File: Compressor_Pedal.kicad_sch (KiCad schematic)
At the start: 14 parts, among them J1 AudioJack2, J2 AudioJack2, U3 LM358, U4 LM358

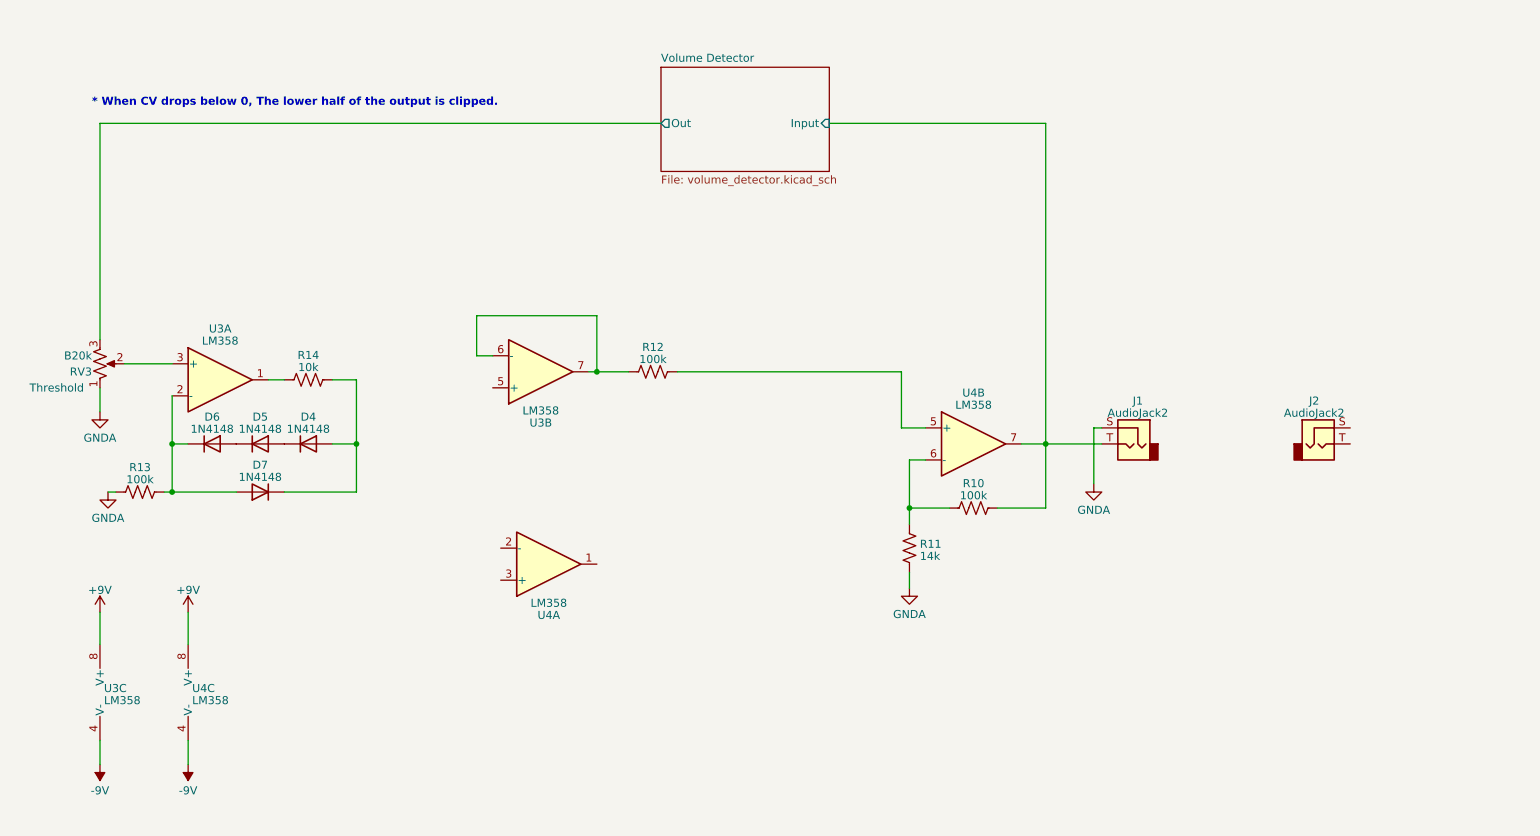
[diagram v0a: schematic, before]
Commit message: schematic finished, begin layout
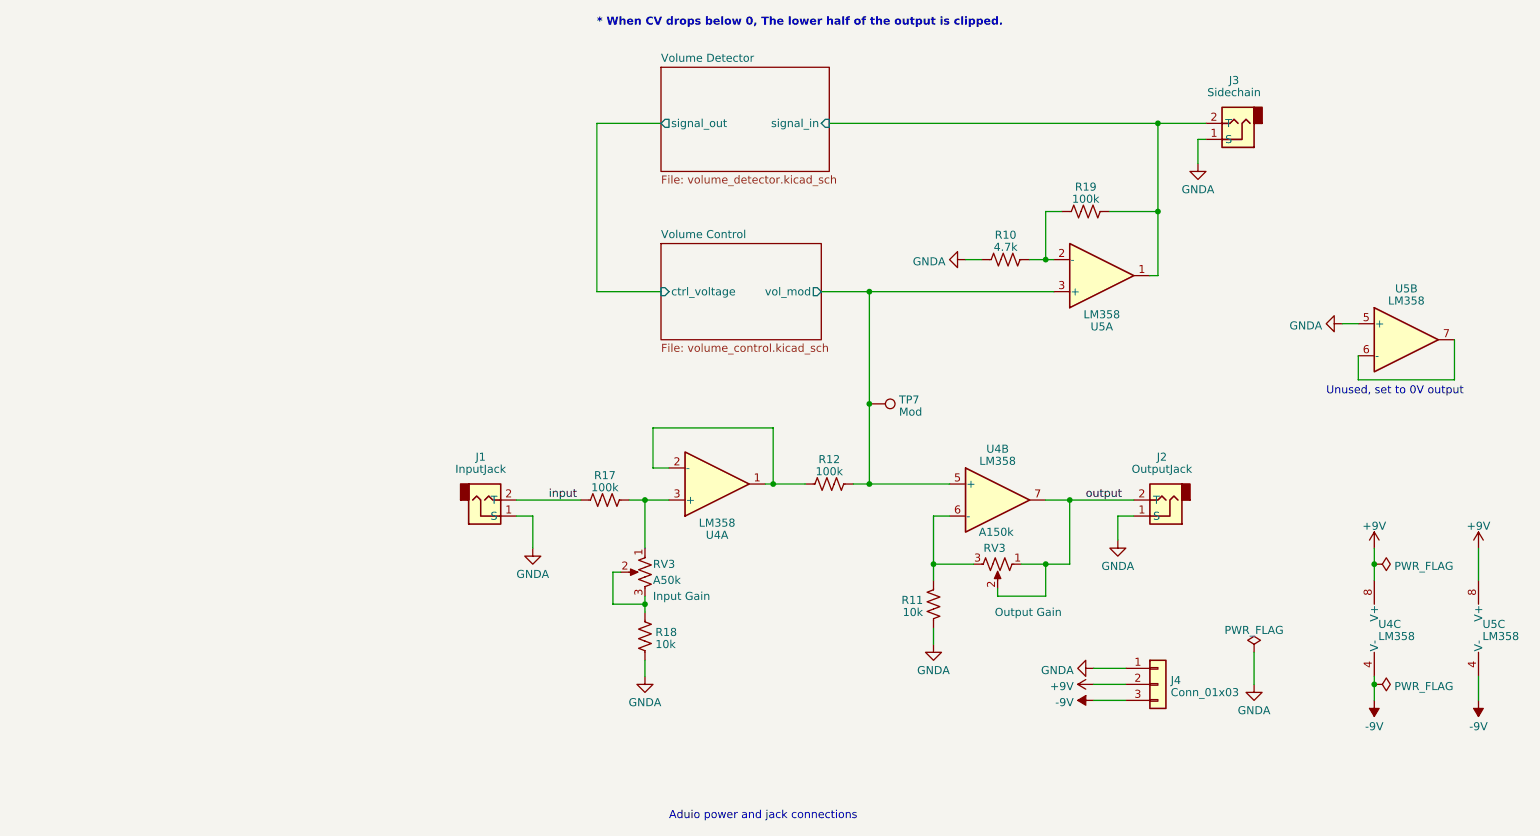
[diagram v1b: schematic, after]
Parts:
- removed D4, D5, D6, D7: 1N4148, Diode_THT:D_DO-35_SOD27_P7.62mm_Horizontal, symbol Diode:1N4148
- removed R13: 100k, symbol Device:R_US
- removed R14: 10k, symbol Device:R_US
- removed RV3: B20k, symbol Device:R_Potentiometer_US
- removed U3: LM358, symbol Amplifier_Operational:LM358
- added J3: Sidechain, TestPoint:TestPoint_2Pads_Pitch5.08mm_Drill1.3mm, symbol Connector_Audio:AudioJack2
- added J4: Conn_01x03, symbol Connector_Generic:Conn_01x03
- added R17, R19: 100k, Resistor_THT:R_Axial_DIN0207_L6.3mm_D2.5mm_P2.54mm_Vertical, symbol Device:R_US
- added R18: 10k, Resistor_THT:R_Axial_DIN0207_L6.3mm_D2.5mm_P2.54mm_Vertical, symbol Device:R_US
- added RV3: A150k, Potentiometer_THT:Potentiometer_Alps_RK163_Single_Horizontal, symbol Device:R_Potentiometer_US
- added RV3: A50k, Potentiometer_THT:Potentiometer_Alps_RK163_Single_Horizontal, symbol Device:R_Potentiometer_US
- added TP7: Mod, Connector_Pin:Pin_D1.3mm_L10.0mm_W3.5mm_Flat, symbol Connector:TestPoint
- added U5: LM358, Package_DIP:DIP-8_W7.62mm_Socket_LongPads, symbol Amplifier_Operational:LM358
- J1: renamed from J2; value AudioJack2 -> InputJack; footprint (none) -> TestPoint:TestPoint_2Pads_Pitch5.08mm_Drill1.3mm
- J2: renamed from J1; value AudioJack2 -> OutputJack; footprint (none) -> TestPoint:TestPoint_2Pads_Pitch5.08mm_Drill1.3mm
- R10: value 100k -> 4.7k; footprint (none) -> Resistor_THT:R_Axial_DIN0207_L6.3mm_D2.5mm_P2.54mm_Vertical
- R11: value 14k -> 10k; footprint (none) -> Resistor_THT:R_Axial_DIN0207_L6.3mm_D2.5mm_P2.54mm_Vertical
- R12: footprint (none) -> Resistor_THT:R_Axial_DIN0207_L6.3mm_D2.5mm_P2.54mm_Vertical
- U4: footprint (none) -> Package_DIP:DIP-8_W7.62mm_Socket_LongPads
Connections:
- net +9V: now also J4.2 (Pin_2), U5.8 (V+)
- net -9V: now also J4.3 (Pin_3), U5.4 (V-)
- net GNDA: now also J1.1 (S), J2.1 (S), R10.1, J3.1 (S), J4.1 (Pin_1), R18.1, U5.5 (+); no longer J2.S
- net at U4.1: now also R12.1, U4.2 (-)
- net at U4.3 (+): now also R17.2, RV3.1
- net Volume Control/vol_mod: now reaches R12.2, U4.5 (+)
- net Volume Control/vol_mod: now also TP7.1, U5.3 (+)
- net at R11.2, U4.6 (-): now also RV3.3; no longer R10.1
- removed net Volume Detector/Input: J2.T, R10.2, U4.7
- new net: R10.2, R19.1, U5.2 (-)
- new net: R18.2, RV3.2, RV3.3
- new net: U5.6 (-), U5.7
- new net Volume Detector/signal_in: J3.2 (T), R19.2, U5.1
- new net input: J1.2 (T), R17.1
- new net output: J2.2 (T), RV3.1, RV3.2, U4.7
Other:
- added sheet Volume Control (volume_control.kicad_sch)
- sheet Volume Detector ports: added signal_in, signal_out; removed Input, Out
- note added: "Aduio power and jack connections"
- note added: "Unused, set to 0V output"
- moved on the sheet: R11, R12, U4A, U4B, U4C

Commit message: sent for build
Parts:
- added JP1, JP2: Jumper_2_Bridged, TestPoint:TestPoint_2Pads_Pitch2.54mm_Drill0.8mm, symbol Jumper:Jumper_2_Bridged
- added TP10: MOD_IN, Connector_Pin:Pin_D0.9mm_L10.0mm_W2.4mm_FlatFork, symbol Connector:TestPoint
- added TP8: AIN, Connector_Pin:Pin_D0.9mm_L10.0mm_W2.4mm_FlatFork, symbol Connector:TestPoint
- added TP9: AOUT, Connector_Pin:Pin_D0.9mm_L10.0mm_W2.4mm_FlatFork, symbol Connector:TestPoint
- J4: footprint (none) -> Connector_PinHeader_2.54mm:PinHeader_1x03_P2.54mm_Vertical
- TP7: value Mod -> MOD_OUT; footprint Connector_Pin:Pin_D1.3mm_L10.0mm_W3.5mm_Flat -> Connector_Pin:Pin_D0.9mm_L10.0mm_W2.4mm_FlatFork
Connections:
- net GNDA: now also JP2.1 (A); no longer U5.5 (+)
- net Volume Detector/signal_in: now also TP10.1
- net input: now also TP8.1
- net output: now also TP9.1
- net at U5.6 (-): now also JP1.1 (A); no longer U5.7
- new net: JP2.2 (B), U5.5 (+)
- new net: JP1.2 (B), U5.7
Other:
- company: (none) -> Jacob Miller
- title: (none) -> Compressor
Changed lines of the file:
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@@
 (kicad_sch (version 20230121) (generator eeschema)
   (paper "A4")
+  (title_block
+    (title "Compressor")
+    (date "2023-05-27")
+    (rev "0.1")
+    (company "Jacob Miller")
+    (comment 4 "All resistors are 1% unless noted")
+  )
   (junction (at 161.29 120.65) (diameter 0) (color 0 0 0 0)
   )
   (junction (at 241.3 152.4) (diameter 0) (color 0 0 0 0)
   )
+  (junction (at 109.22 123.19) (diameter 0) (color 0 0 0 0)
+  )
   (junction (at 125.73 123.19) (diameter 0) (color 0 0 0 0)
   )
@@
   (junction (at 193.04 123.19) (diameter 0) (color 0 0 0 0)
   )
+  (wire (pts (xy 109.22 123.19) (xy 115.57 123.19))
+    (stroke (width 0) (type default))
+  )
   (wire (pts (xy 181.61 138.43) (xy 189.23 138.43))
     (stroke (width 0) (type default))
@@
     (stroke (width 0) (type default))
   )
+  (wire (pts (xy 236.22 95.25) (xy 238.76 95.25))
+    (stroke (width 0) (type default))
+  )
   (wire (pts (xy 207.01 77.47) (xy 207.01 63.5))
     (stroke (width 0) (type default))
@@
     (stroke (width 0) (type default))
   )
-  (wire (pts (xy 254 97.79) (xy 254 104.14))
+  (wire (pts (xy 254 97.79) (xy 254 106.68))
+    (stroke (width 0) (type default))
+  )
+  (wire (pts (xy 109.22 116.84) (xy 109.22 123.19))
+    (stroke (width 0) (type default))
+  )
+  (wire (pts (xy 207.01 58.42) (xy 207.01 63.5))
     (stroke (width 0) (type default))
   )
@@
     (stroke (width 0) (type default))
   )
+  (wire (pts (xy 251.46 106.68) (xy 254 106.68))
+    (stroke (width 0) (type default))
+  )
   (wire (pts (xy 222.25 147.32) (xy 222.25 152.4))
     (stroke (width 0) (type default))
@@
     (stroke (width 0) (type default))
   )
-  (wire (pts (xy 238.76 104.14) (xy 254 104.14))
+  (wire (pts (xy 238.76 106.68) (xy 241.3 106.68))
     (stroke (width 0) (type default))
   )
@@
     (stroke (width 0) (type default))
   )
+  (wire (pts (xy 193.04 118.11) (xy 193.04 123.19))
+    (stroke (width 0) (type default))
+  )
   (wire (pts (xy 127 118.11) (xy 127 111.76))
     (stroke (width 0) (type default))
@@
     (stroke (width 0) (type default))
   )
-  (wire (pts (xy 236.22 95.25) (xy 238.76 95.25))
+  (wire (pts (xy 223.52 95.25) (xy 226.06 95.25))
     (stroke (width 0) (type default))
   )
@@
     (stroke (width 0) (type default))
   )
-  (wire (pts (xy 105.41 123.19) (xy 115.57 123.19))
+  (wire (pts (xy 105.41 123.19) (xy 109.22 123.19))
     (stroke (width 0) (type default))
   )
@@
     (stroke (width 0) (type default))
   )
-  (wire (pts (xy 238.76 100.33) (xy 238.76 104.14))
+  (wire (pts (xy 238.76 100.33) (xy 238.76 106.68))
     (stroke (width 0) (type default))
   )
@@
     (effects (font (size 1.27 1.27) (thickness 0.254) bold) (justify left bottom))
   )
-  (text "Unused, set to 0V output" (at 233.68 106.68 0)
+  (text "Unused, set to 0V output" (at 233.68 87.63 0)
     (effects (font (size 1.27 1.27)) (justify left bottom))
   )
@@
         (path "/a4bfa001-f8c9-4599-807d-bef209d82349"
           (reference "#PWR020") (unit 1)
+        )
+      )
+    )
+  )
+  (symbol (lib_id "Connector:TestPoint") (at 207.01 58.42 0) (unit 1)
+    (in_bom yes) (on_board yes) (dnp no) (fields_autoplaced)
+    (property "Reference" "TP10" (at 208.407 54.4743 0)
+      (effects (font (size 1.27 1.27)) (justify left))
+    )
+    (property "Value" "MOD_IN" (at 208.407 56.3953 0)
+      (effects (font (size 1.27 1.27)) (justify left))
+    )
+    (property "Footprint" "Connector_Pin:Pin_D0.9mm_L10.0mm_W2.4mm_FlatFork" (at 212.09 58.42 0)
+      (effects (font (size 1.27 1.27)) hide)
+    )
+    (property "Datasheet" "~" (at 212.09 58.42 0)
+      (effects (font (size 1.27 1.27)) hide)
+    )
+    (pin "1")
+    (instances
+      (project "Compressor_Pedal"
+        (path "/a4bfa001-f8c9-4599-807d-bef209d82349"
+          (reference "TP10") (unit 1)
         )
       )
@@
     )
   )
+  (symbol (lib_id "Connector:TestPoint") (at 193.04 118.11 0) (unit 1)
+    (in_bom yes) (on_board yes) (dnp no) (fields_autoplaced)
+    (property "Reference" "TP9" (at 194.437 114.1643 0)
+      (effects (font (size 1.27 1.27)) (justify left))
+    )
+    (property "Value" "AOUT" (at 194.437 116.0853 0)
+      (effects (font (size 1.27 1.27)) (justify left))
+    )
+    (property "Footprint" "Connector_Pin:Pin_D0.9mm_L10.0mm_W2.4mm_FlatFork" (at 198.12 118.11 0)
+      (effects (font (size 1.27 1.27)) hide)
+    )
+    (property "Datasheet" "~" (at 198.12 118.11 0)
+      (effects (font (size 1.27 1.27)) hide)
+    )
+    (pin "1")
+    (instances
+      (project "Compressor_Pedal"
+        (path "/a4bfa001-f8c9-4599-807d-bef209d82349"
+          (reference "TP9") (unit 1)
+        )
+      )
+    )
+  )
   (symbol (lib_id "Amplifier_Operational:LM358") (at 243.84 143.51 0) (unit 3)
     (in_bom yes) (on_board yes) (dnp no) (fields_autoplaced)
@@
       (effects (font (size 1.27 1.27)) (justify left))
     )
-    (property "Footprint" "" (at 207.01 152.4 0)
+    (property "Footprint" "Connector_PinHeader_2.54mm:PinHeader_1x03_P2.54mm_Vertical" (at 207.01 152.4 0)
       (effects (font (size 1.27 1.27)) hide)
     )
@@
         (path "/a4bfa001-f8c9-4599-807d-bef209d82349"
           (reference "#PWR032") (unit 1)
+        )
+      )
+    )
+  )
+  (symbol (lib_id "Connector:TestPoint") (at 109.22 116.84 0) (unit 1)
+    (in_bom yes) (on_board yes) (dnp no) (fields_autoplaced)
+    (property "Reference" "TP8" (at 110.617 112.8943 0)
+      (effects (font (size 1.27 1.27)) (justify left))
+    )
+    (property "Value" "AIN" (at 110.617 114.8153 0)
+      (effects (font (size 1.27 1.27)) (justify left))
+    )
+    (property "Footprint" "Connector_Pin:Pin_D0.9mm_L10.0mm_W2.4mm_FlatFork" (at 114.3 116.84 0)
+      (effects (font (size 1.27 1.27)) hide)
+    )
+    (property "Datasheet" "~" (at 114.3 116.84 0)
+      (effects (font (size 1.27 1.27)) hide)
+    )
+    (pin "1")
+    (instances
+      (project "Compressor_Pedal"
+        (path "/a4bfa001-f8c9-4599-807d-bef209d82349"
+          (reference "TP8") (unit 1)
         )
       )
@@
       (effects (font (size 1.27 1.27)) (justify left))
     )
-    (property "Value" "Mod" (at 165.989 109.2273 90)
-      (effects (font (size 1.27 1.27)) (justify left))
-    )
-    (property "Footprint" "Connector_Pin:Pin_D1.3mm_L10.0mm_W3.5mm_Flat" (at 161.29 113.03 0)
+    (property "Value" "MOD_OUT" (at 165.989 109.2273 90)
+      (effects (font (size 1.27 1.27)) (justify left))
+    )
+    (property "Footprint" "Connector_Pin:Pin_D0.9mm_L10.0mm_W2.4mm_FlatFork" (at 161.29 113.03 0)
       (effects (font (size 1.27 1.27)) hide)
     )
@@
     )
   )
+  (symbol (lib_id "Jumper:Jumper_2_Bridged") (at 246.38 106.68 0) (unit 1)
+    (in_bom yes) (on_board yes) (dnp no)
+    (property "Reference" "JP1" (at 246.38 104.14 0)
+      (effects (font (size 1.27 1.27)))
+    )
+    (property "Value" "Jumper_2_Bridged" (at 246.38 109.22 0)
+      (effects (font (size 1.27 1.27)))
+    )
+    (property "Footprint" "TestPoint:TestPoint_2Pads_Pitch2.54mm_Drill0.8mm" (at 246.38 106.68 0)
+      (effects (font (size 1.27 1.27)) hide)
+    )
+    (property "Datasheet" "~" (at 246.38 106.68 0)
+      (effects (font (size 1.27 1.27)) hide)
+    )
+    (pin "1")
+    (pin "2")
+    (instances
+      (project "Compressor_Pedal"
+        (path "/a4bfa001-f8c9-4599-807d-bef209d82349"
+          (reference "JP1") (unit 1)
+        )
+      )
+    )
+  )
   (symbol (lib_id "Device:R_US") (at 171.45 139.7 0) (mirror x) (unit 1)
     (in_bom yes) (on_board yes) (dnp no)
@@
     )
   )
-  (symbol (lib_id "power:GNDA") (at 236.22 95.25 270) (unit 1)
-    (in_bom yes) (on_board yes) (dnp no) (fields_autoplaced)
-    (property "Reference" "#PWR027" (at 229.87 95.25 0)
-      (effects (font (size 1.27 1.27)) hide)
-    )
-    (property "Value" "GNDA" (at 233.0451 95.5668 90)
+  (symbol (lib_id "power:GNDA") (at 223.52 95.25 270) (unit 1)
+    (in_bom yes) (on_board yes) (dnp no) (fields_autoplaced)
+    (property "Reference" "#PWR027" (at 217.17 95.25 0)
+      (effects (font (size 1.27 1.27)) hide)
+    )
+    (property "Value" "GNDA" (at 220.3451 95.5668 90)
       (effects (font (size 1.27 1.27)) (justify right))
     )
-    (property "Footprint" "" (at 236.22 95.25 0)
-      (effects (font (size 1.27 1.27)) hide)
-    )
-    (property "Datasheet" "" (at 236.22 95.25 0)
+    (property "Footprint" "" (at 223.52 95.25 0)
+      (effects (font (size 1.27 1.27)) hide)
+    )
+    (property "Datasheet" "" (at 223.52 95.25 0)
       (effects (font (size 1.27 1.27)) hide)
     )
@@
         )
       )
+    )
+  )
+  (symbol (lib_id "Jumper:Jumper_2_Bridged") (at 231.14 95.25 0) (unit 1)
+    (in_bom yes) (on_board yes) (dnp no)
+    (property "Reference" "JP2" (at 231.14 92.71 0)
+      (effects (font (size 1.27 1.27)))
+    )
+    (property "Value" "Jumper_2_Bridged" (at 231.14 97.79 0)
+      (effects (font (size 1.27 1.27)))
+    )
+    (property "Footprint" "TestPoint:TestPoint_2Pads_Pitch2.54mm_Drill0.8mm" (at 231.14 95.25 0)
+      (effects (font (size 1.27 1.27)) hide)
+    )
+    (property "Datasheet" "~" (at 231.14 95.25 0)
+      (effects (font (size 1.27 1.27)) hide)
+    )
+    (pin "1")
+    (pin "2")
+    (instances
+      (project "Compressor_Pedal"
+        (path "/a4bfa001-f8c9-4599-807d-bef209d82349"
+          (reference "JP2") (unit 1)
+        )
+      )
